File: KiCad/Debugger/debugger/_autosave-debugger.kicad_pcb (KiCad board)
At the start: 2 copper layers, 97 x 53.3 mm, 22 parts, among them J1 Conn_02x18_Odd_Even, J10 Conn_01x08, J11 Conn_01x08, J12 Conn_01x08, J13 Conn_01x08, J14 Conn_01x08, J15 Conn_01x10, J16 Conn_01x10, J17 Conn_01x10, J18 Conn_01x08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

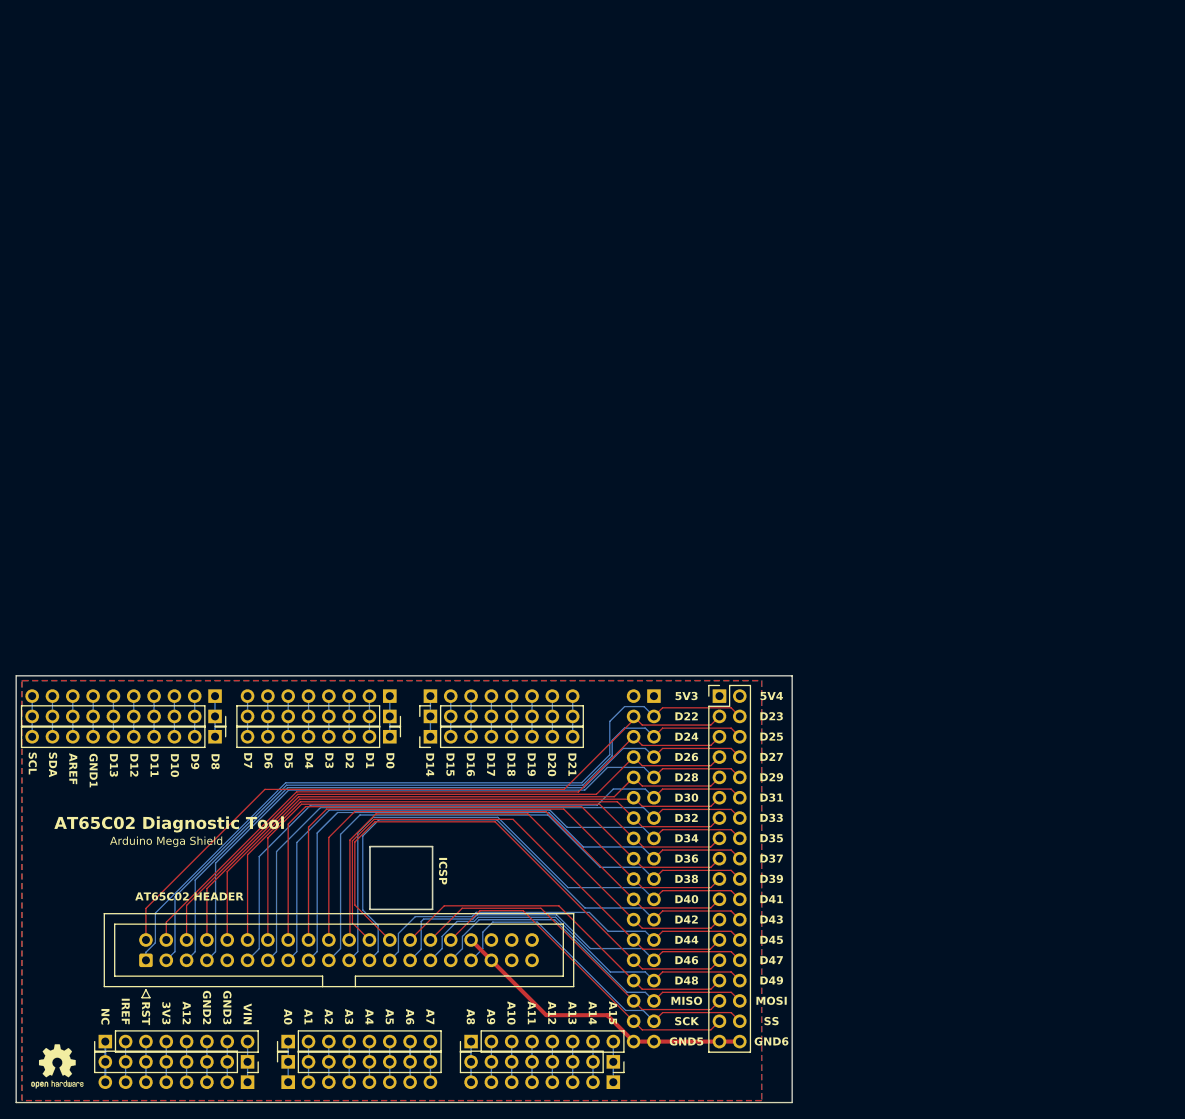
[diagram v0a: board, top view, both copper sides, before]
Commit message: Silkscreen Updates
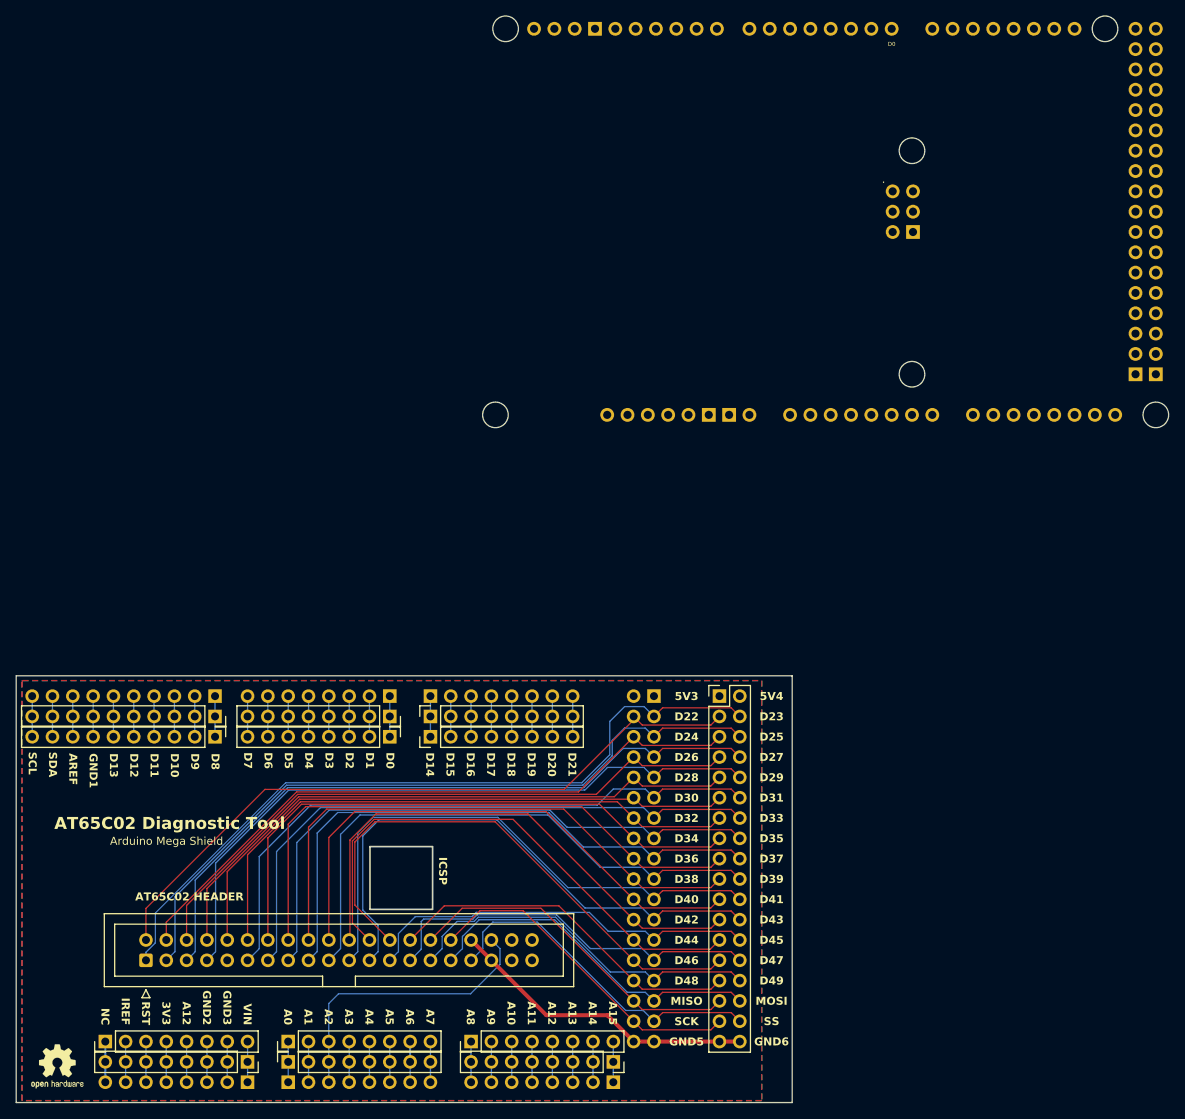
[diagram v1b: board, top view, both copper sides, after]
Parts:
- added XA1: Arduino_Mega2560_Shield, PCM_arduino-library:Arduino_Mega2560_Shield, F.Cu at (70.5, -47.3)
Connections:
- J11 pad 3: Net-(J11-Pin_3) -> CLK
- J2 pad 36: unconnected-(J2-Pin_36-Pad36) -> CLK
- J3 pad 3: Net-(J11-Pin_3) -> CLK
- J7 pad 3: Net-(J11-Pin_3) -> CLK
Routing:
- net CLK: track 0.00 -> 36.8 mm
- net Net-(J11-Pin_3): track 5.08 -> 0.00 mm
